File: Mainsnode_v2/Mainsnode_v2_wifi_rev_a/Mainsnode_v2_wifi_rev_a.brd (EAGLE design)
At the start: 72.6 x 47.1 mm, 49 parts, among them J2 WIRE_HOLE-14AWG, J3 WIRE_HOLE-14AWG, J4 HOLE, J5 HOLE, J6 HOLE, J7 HOLE, K1 S216S01F, Q3 MMBT2222A

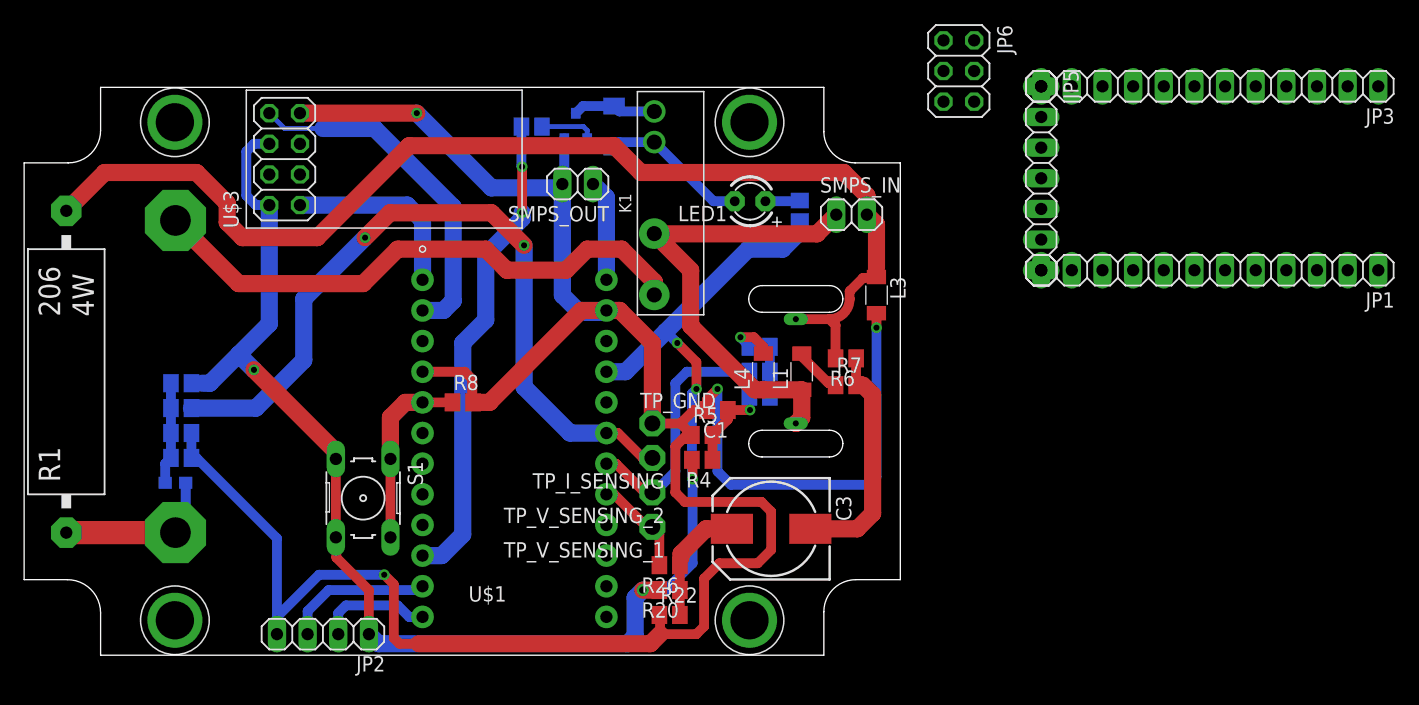
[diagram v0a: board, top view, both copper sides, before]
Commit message: updt wifi brd rev a (rmv cmpnents)
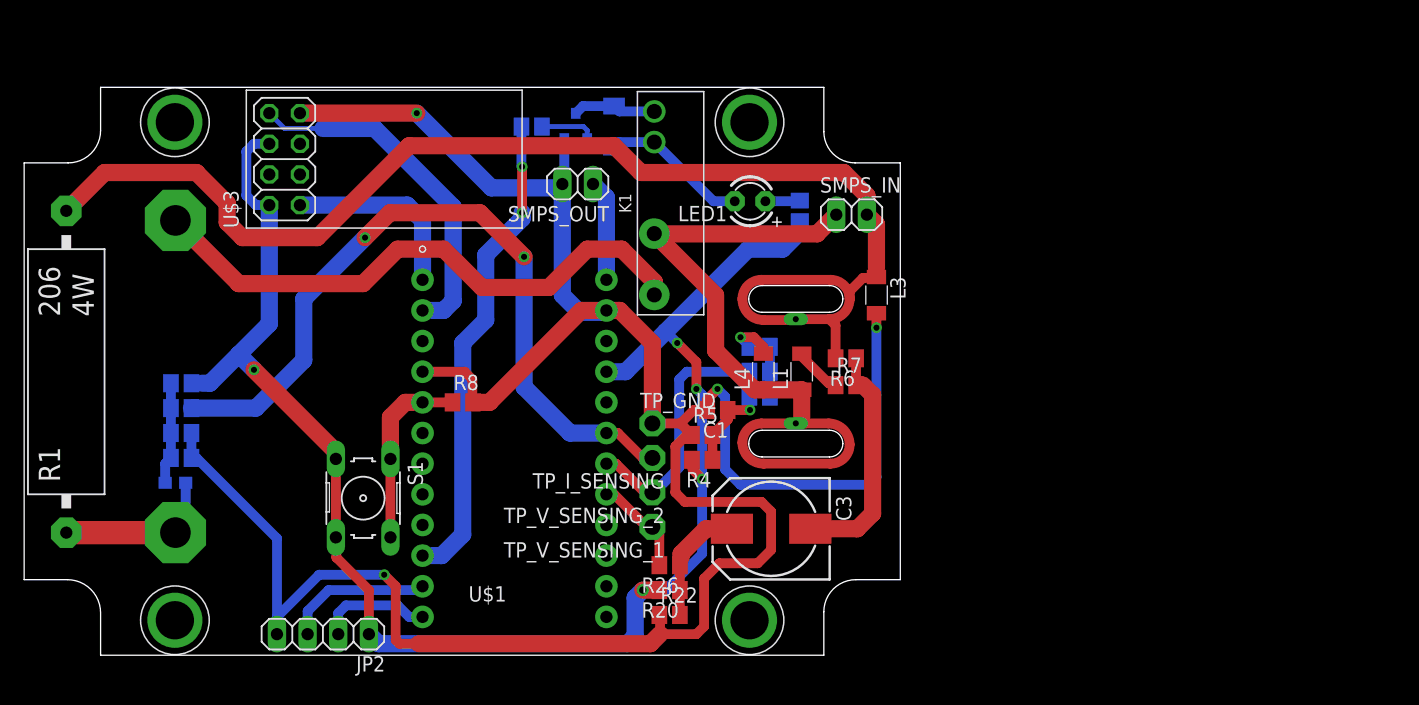
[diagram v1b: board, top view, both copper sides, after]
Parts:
- removed JP1, JP3: (no value), pinhead:1X12
- removed JP5: (no value), pinhead:1X07
- removed JP6: (no value), pinhead:2X03
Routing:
- net WALL_PHASE: track 39.0 -> 58.7 mm
- net WALL_NEUTRAL: track 94.7 -> 110.3 mm
- net LOAD_PHASE: track 46.7 -> 47.9 mm
- net 3V3: track 131.0 -> 131.6 mm
- net I_SENSING: track 63.2 -> 62.6 mm
